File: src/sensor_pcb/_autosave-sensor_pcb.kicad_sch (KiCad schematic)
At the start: 29 parts, among them IC1 TCAN3414DRBR, J1 66200421024, J2 643280100305, J3 66200821024, J4 643280100305, J5 66200821024, J7 66200421024, U1 SHT45-AD1B, U2 16-bit ADC, U4 BMP581

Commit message: tuesday changes
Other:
- note added: "Check footprint!"
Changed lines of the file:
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@@
 		)
 	)
+	(text "Check footprint!\n"
+		(exclude_from_sim no)
+		(at 205.486 152.146 0)
+		(effects
+			(font
+				(size 1.27 1.27)
+			)
+		)
+	)
 	(text "CAN Connector 1\n"
 		(exclude_from_sim no)
@@
 			)
 		)
-		(property "Description" "Board Mount Humidity Sensors Digital Humidity and Temperature Sensor incl Filter Membrane"
+		(property "Description" "Board Mount Humidity Sensors Digital Humidity and TemperaturLowe Sensor incl Filter Membrane"
 			(at 231.14 133.35 0)
 			(effects

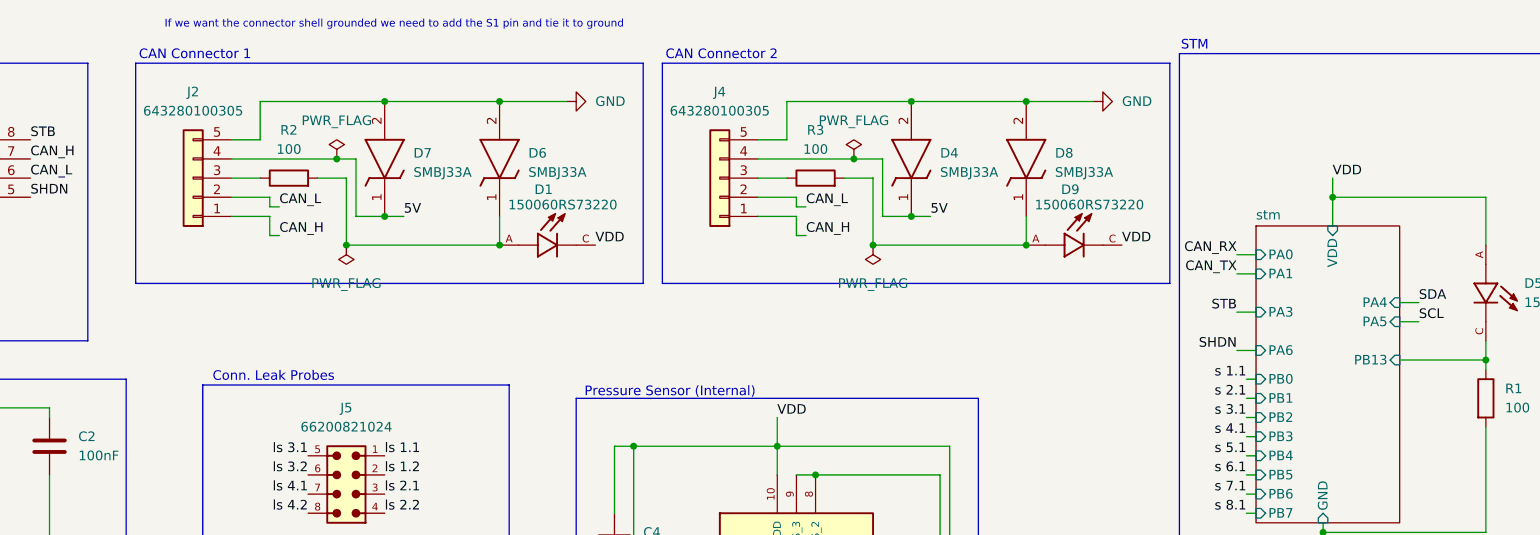
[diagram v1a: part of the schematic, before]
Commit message: fixing up parts according to kicad auto errors
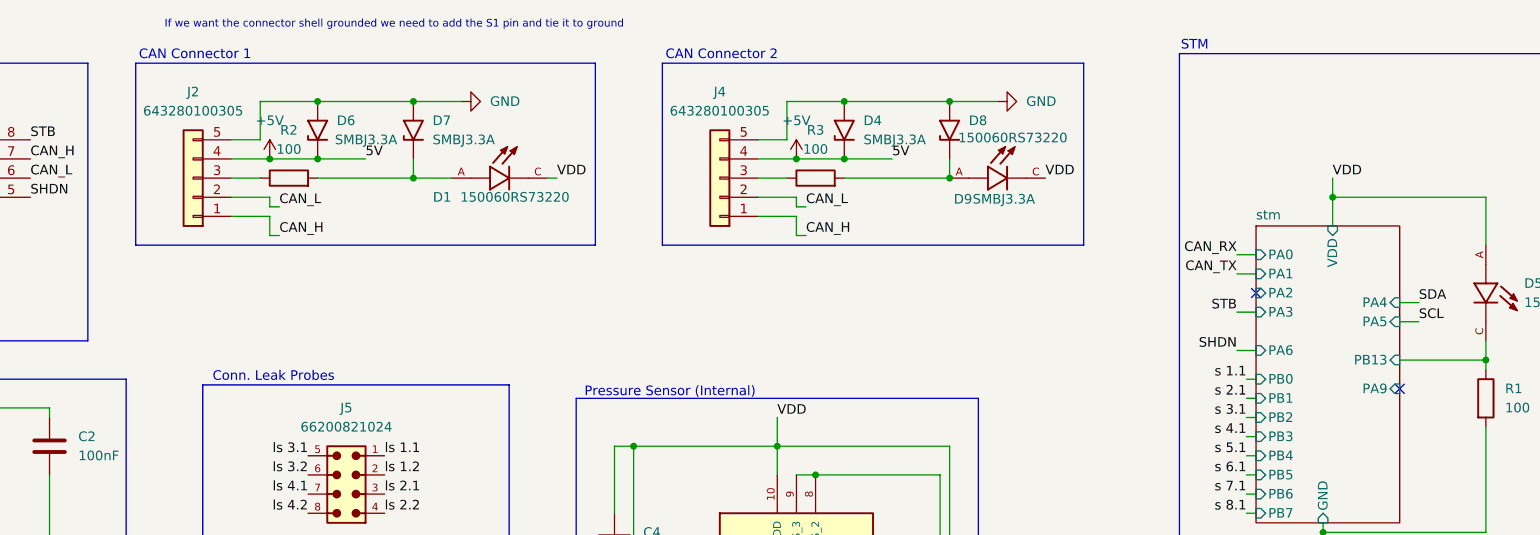
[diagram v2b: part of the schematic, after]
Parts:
- removed D4, D6, D7, D8: SMBJ33A, DIOM5436X244N, symbol dz_dio:SMBJ33A
- added D4, D6, D7, D8: SMBJ3.3A, Diode_SMD:D_SMB, symbol #dzdb:s_dio/D-TVS-SMBJ3V3
- U4: footprint dz_sens:BMP581 -> dz_sens:QFN10_BMP581_BOS
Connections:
- net GND: now also D4.2 (A2), D6.2 (A2), D7.2 (A2), D8.2 (A2)
- net at D1.A, R2.2: now also D7.1 (A1)
- net at D9.A, R3.2: now also D8.1 (A1)
- net 5V renamed +5V
- net +5V: now also D4.1 (A1), D6.1 (A1)
- no-connect marks 6 -> 8
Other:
- sheet stm ports: added PA2, PA9; removed none
- moved on the sheet: D1, D9
